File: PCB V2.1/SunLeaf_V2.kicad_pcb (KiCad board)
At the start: 4 copper layers, 77 x 40 mm, 107 parts, among them IC1 ESP_09, J1 20021121-00010C4LF, J10 B4B-PH-K-S(LF)(SN), J11 B4B-PH-K-S(LF)(SN), J12 B4B-PH-K-S(LF)(SN), J13 B4B-PH-K-S(LF)(SN), J14 B4B-PH-K-S(LF)(SN), J15 B4B-PH-K-S(LF)(SN), J16 B4B-PH-K-S(LF)(SN), J2 0475890001-MicroUSBPort, J3 B2B-PH-K-S(LF)(SN), J4 B3B-PH-K-S(LF)(SN), J5 B4B-PH-K-S(LF)(SN), J6 B4B-PH-K-S(LF)(SN), J7 B4B-PH-K-S(LF)(SN), J8 B4B-PH-K-S(LF)(SN), J9 B4B-PH-K-S(LF)(SN), P1 CONN_01X04, Q1 DMG2307L-7, Q2 DMG2307L-7, SW1 B3U-1000P, SW2 B3U-1000P, T1 1909763-1, U1 STM32F446RET6_-_TQFP64, U2 BQ24210DQCT, U3 AZ1117CR-3.3TRG1_1, U4 74HC4052D, U5 PCA9518DBQR, X1 ABM3B8.000MHZB2T, X2 ABS07-32.768KHZ-9-T

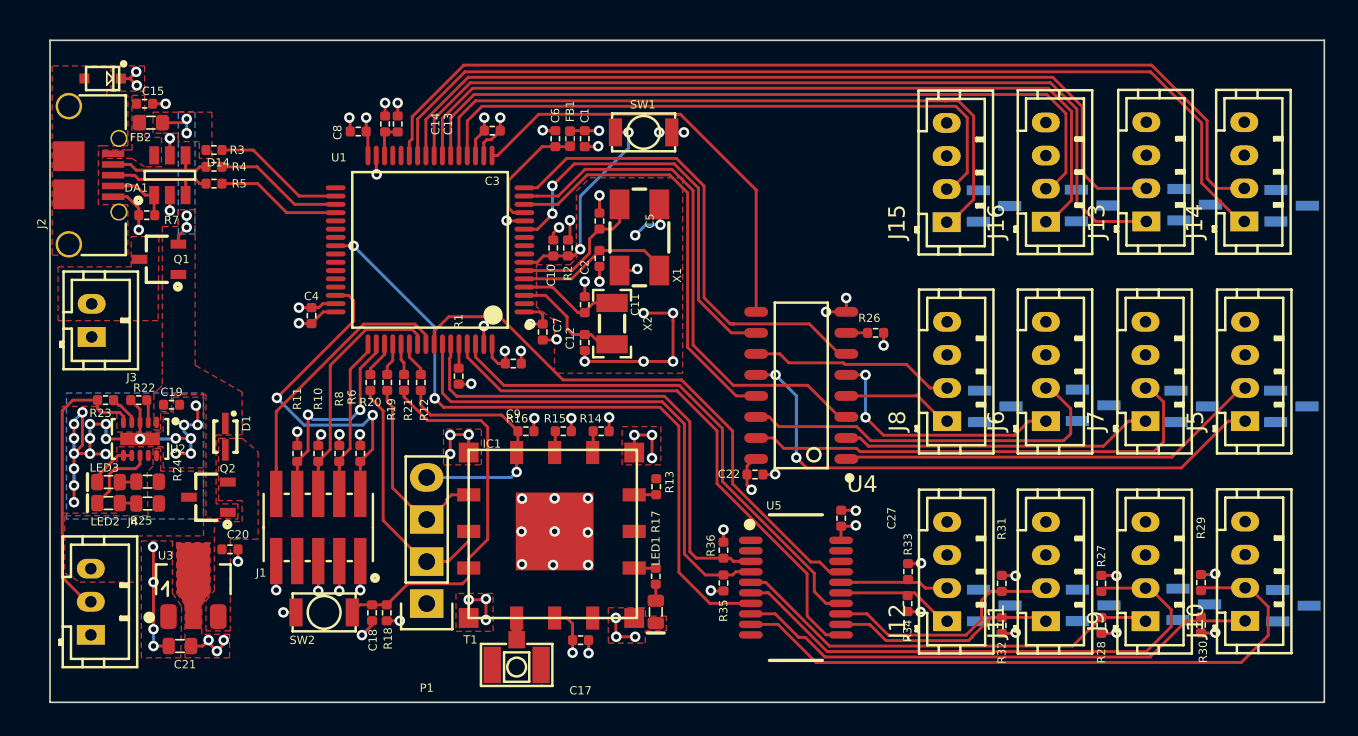
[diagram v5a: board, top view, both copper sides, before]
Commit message: Internal Planes
Internal Planes added, small amount of routing left.
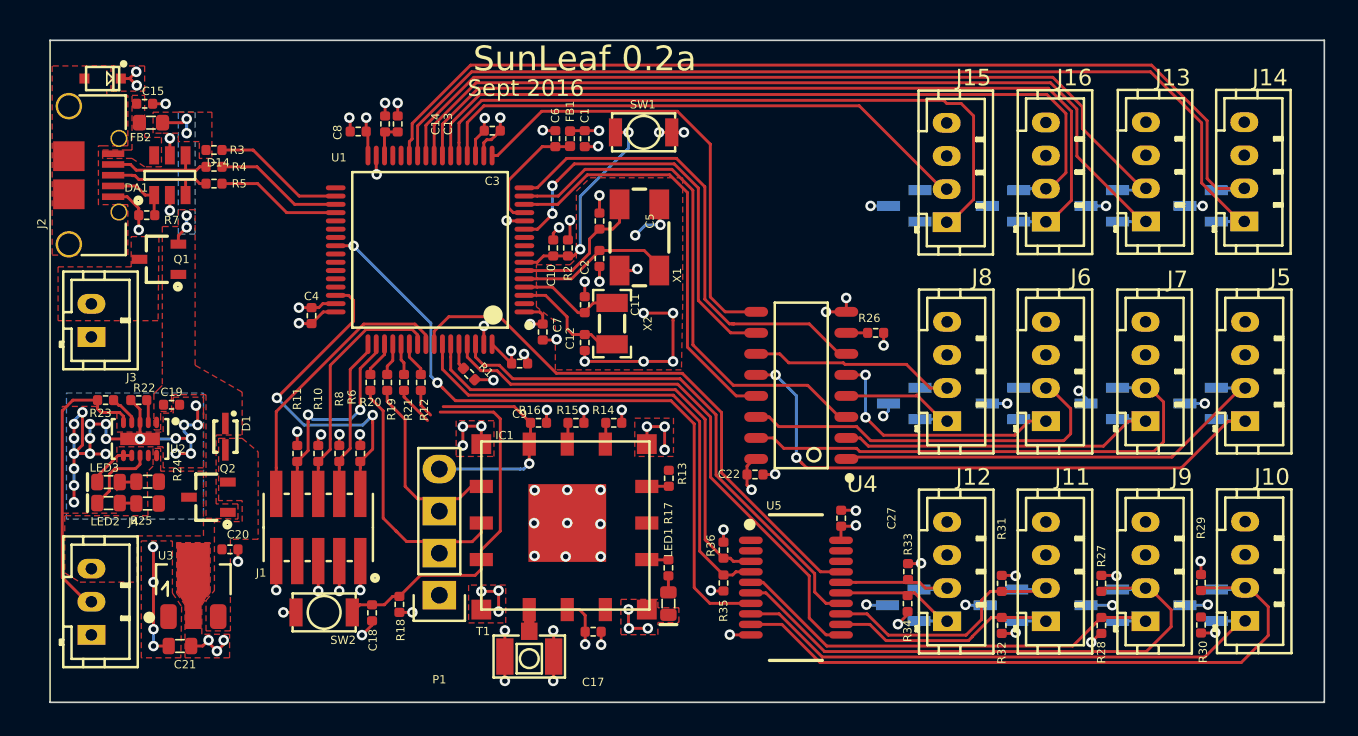
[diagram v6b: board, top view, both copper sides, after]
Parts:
- moved D13 5.61 mm to (106.6, 40.0), turned to 180 degrees
- moved D7 5.61 mm to (112.5, 64.1), turned to 180 degrees
- moved D8 5.57 mm to (100.5, 64.1), turned to 180 degrees
- moved D6 5.56 mm to (106.6, 64.1), turned to 180 degrees
- moved D2 5.51 mm to (94.6, 51.9), turned to 180 degrees
- moved D9 5.51 mm to (94.6, 64.1), turned to 180 degrees
- moved D12 5.50 mm to (112.5, 40.0), turned to 180 degrees
- moved D5 5.49 mm to (112.5, 51.9), turned to 180 degrees
- moved D4 5.45 mm to (100.6, 51.9), turned to 180 degrees
- moved D3 5.44 mm to (106.6, 51.9), turned to 180 degrees
- moved D11 5.43 mm to (94.6, 40.0), turned to 180 degrees
- moved D10 5.38 mm to (100.6, 40.0), turned to 180 degrees
- moved IC1 0.92 mm to (69.1, 64.4)
- moved R18 0.92 mm to (64.1, 64.1)
- moved P1 0.92 mm to (66.5, 63.5)
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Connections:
- D10 pad 1: /Analog and Digital Grove IO/ANIO_7 -> /Analog and Digital Grove IO/ANIO_6
- D10 pad 2: /Analog and Digital Grove IO/ANIO_6 -> /Analog and Digital Grove IO/ANIO_7
- D11 pad 1: /Analog and Digital Grove IO/ANIO_5 -> /Analog and Digital Grove IO/ANIO_4
- D11 pad 2: /Analog and Digital Grove IO/ANIO_4 -> /Analog and Digital Grove IO/ANIO_5
- D12 pad 1: /Analog and Digital Grove IO/ANIO_3 -> /Analog and Digital Grove IO/ANIO_2
- D12 pad 2: /Analog and Digital Grove IO/ANIO_2 -> /Analog and Digital Grove IO/ANIO_3
- D13 pad 1: /Analog and Digital Grove IO/ANIO_1 -> /Analog and Digital Grove IO/ANIO_0
- D13 pad 2: /Analog and Digital Grove IO/ANIO_0 -> /Analog and Digital Grove IO/ANIO_1
- D2 pad 1: /UART Grove Sensors/UART_RX3 -> /UART Grove Sensors/UART_TX3
- D2 pad 2: /UART Grove Sensors/UART_TX3 -> /UART Grove Sensors/UART_RX3
- D3 pad 1: /UART Grove Sensors/UART_RX2 -> /UART Grove Sensors/UART_TX2
- D3 pad 2: /UART Grove Sensors/UART_TX2 -> /UART Grove Sensors/UART_RX2
- D4 pad 1: /UART Grove Sensors/UART_RX1 -> /UART Grove Sensors/UART_TX1
- D4 pad 2: /UART Grove Sensors/UART_TX1 -> /UART Grove Sensors/UART_RX1
- D5 pad 1: /UART Grove Sensors/UART_RX0 -> /UART Grove Sensors/UART_TX0
- D5 pad 2: /UART Grove Sensors/UART_TX0 -> /UART Grove Sensors/UART_RX0
- J10 pad 1: Net-(D7-Pad1) -> Net-(D7-Pad2)
- J10 pad 2: Net-(D7-Pad2) -> Net-(D7-Pad1)
- J11 pad 1: Net-(D8-Pad1) -> Net-(D8-Pad2)
- J11 pad 2: Net-(D8-Pad2) -> Net-(D8-Pad1)
- J12 pad 1: Net-(D9-Pad1) -> Net-(D9-Pad2)
- J12 pad 2: Net-(D9-Pad2) -> Net-(D9-Pad1)
- J9 pad 1: Net-(D6-Pad1) -> Net-(D6-Pad2)
- J9 pad 2: Net-(D6-Pad2) -> Net-(D6-Pad1)
- R27 pad 2: Net-(D6-Pad2) -> Net-(D6-Pad1)
- R28 pad 2: Net-(D6-Pad1) -> Net-(D6-Pad2)
- R29 pad 2: Net-(D7-Pad2) -> Net-(D7-Pad1)
- R30 pad 2: Net-(D7-Pad1) -> Net-(D7-Pad2)
- R31 pad 2: Net-(D8-Pad2) -> Net-(D8-Pad1)
- R32 pad 2: Net-(D8-Pad1) -> Net-(D8-Pad2)
- R33 pad 2: Net-(D9-Pad2) -> Net-(D9-Pad1)
- R34 pad 2: Net-(D9-Pad1) -> Net-(D9-Pad2)
- U5 pad 12: Net-(D8-Pad1) -> Net-(D8-Pad2)
- U5 pad 13: Net-(D8-Pad2) -> Net-(D8-Pad1)
- U5 pad 15: Net-(D9-Pad1) -> Net-(D9-Pad2)
- U5 pad 16: Net-(D9-Pad2) -> Net-(D9-Pad1)
- U5 pad 5: Net-(D6-Pad1) -> Net-(D6-Pad2)
- U5 pad 6: Net-(D6-Pad2) -> Net-(D6-Pad1)
- U5 pad 8: Net-(D7-Pad1) -> Net-(D7-Pad2)
- U5 pad 9: Net-(D7-Pad2) -> Net-(D7-Pad1)
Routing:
- net GND: track 120.2 -> 139.3 mm, vias 92 -> 107
- net Net-(D7-Pad1): track 31.9 -> 41.0 mm
- net Net-(D6-Pad1): track 26.3 -> 35.1 mm
- net Net-(D7-Pad2): track 39.2 -> 33.6 mm
- net Net-(D6-Pad2): track 33.4 -> 28.0 mm
- net /Analog and Digital Grove IO/ANIO_4: track 38.0 -> 33.5 mm
- net Net-(D8-Pad1): track 13.5 -> 16.6 mm
- net Net-(D9-Pad2): track 6.73 -> 8.83 mm
- net /UART Grove Sensors/UART_RX0: track 35.4 -> 37.2 mm
- net /UART Grove Sensors/UART_TX0: track 26.0 -> 27.7 mm
- net /UART Grove Sensors/UART_RX2: track 19.0 -> 20.8 mm
- net /UART Grove Sensors/UART_TX2: track 29.2 -> 30.9 mm
- net /UART Grove Sensors/UART_RX3: track 6.88 -> 8.57 mm
- net /UART Grove Sensors/UART_TX3: track 12.5 -> 14.2 mm
- net Net-(D6-Pad3): track 0.00 -> 1.59 mm, vias 0 -> 1
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- added copper zone on In2.Cu, net +3V3
- added copper zone on In1.Cu, net GND
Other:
- board text added: "Sept 2016"
- board text added: "SunLeaf 0.2a"

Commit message: PDF
Schematic PDF updated.
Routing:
- net Net-(C18-Pad1): track 24.6 -> 25.3 mm
- net /WiFi-ESP8266-ESP-09/PGM_MODE: track 15.5 -> 16.1 mm
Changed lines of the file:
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@@
     (thickness 1.6)
     (drawings 16)
-    (tracks 1002)
+    (tracks 1004)
     (zones 0)
     (modules 107)
@@
   (segment (start 63.208829 36.957872) (end 63.211457 36.9605) (width 0.1778) (layer F.Cu) (net 9))
   (segment (start 64.008 35.535) (end 63.246 35.535) (width 0.1778) (layer F.Cu) (net 9))
-  (segment (start 64.1096 63.6008) (end 63.7046 63.6008) (width 0.1778) (layer F.Cu) (net 11))
-  (segment (start 63.7046 63.6008) (end 63.1966 64.1088) (width 0.1778) (layer F.Cu) (net 11))
-  (segment (start 63.1966 64.1088) (end 62.4586 64.1088) (width 0.1778) (layer F.Cu) (net 11))
-  (segment (start 64.389 51.156) (end 64.389 51.54744) (width 0.1778) (layer F.Cu) (net 11))
-  (segment (start 64.389 51.54744) (end 65.812713 52.971153) (width 0.1778) (layer F.Cu) (net 11))
-  (segment (start 66.574713 52.463153) (end 69.801567 52.463153) (width 0.1778) (layer F.Cu) (net 11))
+  (segment (start 64.389 51.156) (end 64.389 51.788336) (width 0.1778) (layer F.Cu) (net 11))
+  (segment (start 64.389 51.788336) (end 65.063817 52.463153) (width 0.1778) (layer F.Cu) (net 11))
+  (segment (start 65.063817 52.463153) (end 69.801567 52.463153) (width 0.1778) (layer F.Cu) (net 11))
   (segment (start 69.801567 52.463153) (end 70.205528 52.867114) (width 0.1778) (layer F.Cu) (net 11))
   (segment (start 70.205528 52.867114) (end 70.205528 59.651772) (width 0.1778) (layer F.Cu) (net 11))
   (segment (start 70.205528 59.651772) (end 69.0601 60.7972) (width 0.1778) (layer F.Cu) (net 11))
   (segment (start 69.0601 60.7972) (end 69.0601 61.375) (width 0.1778) (layer F.Cu) (net 11))
+  (segment (start 64.1096 63.6008) (end 63.7046 63.6008) (width 0.1778) (layer F.Cu) (net 11))
+  (segment (start 63.7046 63.6008) (end 63.1966 64.1088) (width 0.1778) (layer F.Cu) (net 11))
+  (segment (start 63.1966 64.1088) (end 62.4586 64.1088) (width 0.1778) (layer F.Cu) (net 11))
   (segment (start 69.0601 61.375) (end 69.0601 61.9528) (width 0.1778) (layer F.Cu) (net 11))
   (segment (start 69.0601 61.9528) (end 68.6813 62.3316) (width 0.1778) (layer F.Cu) (net 11))
@@
   (segment (start 74.2946 53.1114) (end 74.2946 54.3575) (width 0.1778) (layer F.Cu) (net 39))
   (segment (start 74.2946 54.3575) (end 74.2541 54.398) (width 0.1778) (layer F.Cu) (net 39))
-  (segment (start 72.0336 53.1114) (end 71.055142 52.132942) (width 0.1778) (layer F.Cu) (net 40))
-  (segment (start 71.055142 52.132942) (end 66.757778 52.132942) (width 0.1778) (layer F.Cu) (net 40))
-  (segment (start 65.995778 52.640942) (end 65.405 52.050164) (width 0.1778) (layer F.Cu) (net 40))
-  (segment (start 65.405 52.050164) (end 65.405 51.156) (width 0.1778) (layer F.Cu) (net 40))
-  (segment (start 71.9582 55.5752) (end 71.626994 55.906406) (width 0.1778) (layer B.Cu) (net 40))
-  (segment (start 71.626994 55.906406) (end 71.41671 55.906406) (width 0.1778) (layer B.Cu) (net 40))
-  (segment (start 71.41671 55.906406) (end 71.415704 55.9054) (width 0.1778) (layer B.Cu) (net 40))
-  (segment (start 71.415704 55.9054) (end 66.5226 55.9054) (width 0.1778) (layer B.Cu) (net 40))
+  (segment (start 71.9582 55.5752) (end 71.415723 56.117677) (width 0.1778) (layer B.Cu) (net 40))
+  (segment (start 71.415723 56.117677) (end 66.734877 56.117677) (width 0.1778) (layer B.Cu) (net 40))
+  (segment (start 66.734877 56.117677) (end 66.5226 55.9054) (width 0.1778) (layer B.Cu) (net 40))
+  (segment (start 71.12 52.1978) (end 71.055143 52.132943) (width 0.1778) (layer F.Cu) (net 40))
+  (segment (start 71.055143 52.132943) (end 65.803768 52.132943) (width 0.1778) (layer F.Cu) (net 40))
+  (segment (start 65.803768 52.132943) (end 65.397642 51.726817) (width 0.1778) (layer F.Cu) (net 40))
+  (segment (start 65.397642 51.726817) (end 65.397642 51.163358) (width 0.1778) (layer F.Cu) (net 40))
+  (segment (start 65.397642 51.163358) (end 65.405 51.156) (width 0.1778) (layer F.Cu) (net 40))
+  (segment (start 72.0336 53.1114) (end 71.12 52.1978) (width 0.1778) (layer F.Cu) (net 40))
+  (segment (start 71.12 52.1978) (end 71.055142 52.132942) (width 0.1778) (layer F.Cu) (net 40))
   (segment (start 71.9561 54.398) (end 71.9561 55.5731) (width 0.1778) (layer F.Cu) (net 40))
   (segment (start 71.9561 55.5731) (end 71.9582 55.5752) (width 0.1778) (layer F.Cu) (net 40))

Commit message: Workstation Switch
Switching to laptop, syncing files.
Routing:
- net /MCU-STM32F446RET6/ESP_ST_RST: track 12.8 -> 52.2 mm
- net GND: track 139.3 -> 140.4 mm
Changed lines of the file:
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@@
     (thickness 1.6)
     (drawings 16)
-    (tracks 1004)
+    (tracks 1021)
     (zones 0)
     (modules 107)
@@
   (segment (start 52.2224 66.5988) (end 52.578 66.2432) (width 0.1778) (layer F.Cu) (net 1))
   (via (at 52.578 66.2432) (size 0.635) (drill 0.3302) (layers F.Cu B.Cu) (net 1))
+  (segment (start 69.211457 48.3605) (end 69.211457 47.783923) (width 0.1778) (layer F.Cu) (net 2))
+  (segment (start 69.211457 47.783923) (end 69.560537 47.434843) (width 0.1778) (layer F.Cu) (net 2))
+  (segment (start 69.560537 47.434843) (end 69.929908 47.434843) (width 0.1778) (layer F.Cu) (net 2))
+  (segment (start 69.929908 47.434843) (end 70.132146 47.637081) (width 0.1778) (layer F.Cu) (net 2))
+  (segment (start 70.132146 47.637081) (end 70.449645 47.95458) (width 0.1778) (layer F.Cu) (net 2))
+  (via (at 70.449645 47.95458) (size 0.635) (drill 0.3302) (layers F.Cu B.Cu) (net 2))
   (segment (start 99.634 51.943) (end 100.838 51.943) (width 0.1778) (layer B.Cu) (net 2))
   (via (at 100.838 51.943) (size 0.635) (drill 0.3302) (layers F.Cu B.Cu) (net 2))
@@
   (via (at 86.8172 56.2102) (size 0.635) (drill 0.3302) (layers F.Cu B.Cu) (net 2))
   (segment (start 69.0601 64.398) (end 69.0601 63.2993) (width 0.1778) (layer F.Cu) (net 2))
-  (segment (start 69.0601 63.2993) (end 69.0626 63.2968) (width 0.1778) (layer F.Cu) (net 2))
   (via (at 69.0626 63.2968) (size 0.635) (drill 0.3302) (layers F.Cu B.Cu) (net 2))
   (via (at 79.0702 53.34) (size 0.635) (drill 0.3302) (layers F.Cu B.Cu) (net 2))
@@
   (segment (start 57.863 64.5668) (end 57.0992 64.5668) (width 0.1778) (layer F.Cu) (net 2))
   (via (at 57.0992 64.5668) (size 0.635) (drill 0.3302) (layers F.Cu B.Cu) (net 2))
-  (via (at 69.215 47.25735) (size 0.635) (drill 0.3302) (layers F.Cu B.Cu) (net 2))
-  (segment (start 69.211457 47.260893) (end 69.215 47.25735) (width 0.1778) (layer F.Cu) (net 2))
-  (segment (start 69.211457 48.3605) (end 69.211457 47.260893) (width 0.1778) (layer F.Cu) (net 2))
   (segment (start 73.569721 48.108) (end 73.61118 48.066541) (width 0.1778) (layer F.Cu) (net 2))
   (segment (start 72.771 48.108) (end 73.569721 48.108) (width 0.1778) (layer F.Cu) (net 2))
@@
   (segment (start 73.533 36.424) (end 74.394 36.424) (width 0.1778) (layer F.Cu) (net 5))
   (segment (start 74.394 36.424) (end 74.422 36.396) (width 0.1778) (layer F.Cu) (net 5))
+  (segment (start 80.391 55.9808) (end 80.237799 56.134001) (width 0.1778) (layer F.Cu) (net 6))
+  (segment (start 55.372 60.552058) (end 56.488058 59.436) (width 0.1778) (layer F.Cu) (net 6))
+  (segment (start 56.488058 59.436) (end 56.642 59.436) (width 0.1778) (layer F.Cu) (net 6))
+  (segment (start 80.237799 56.134001) (end 71.881999 56.134001) (width 0.1778) (layer F.Cu) (net 6))
+  (segment (start 71.881999 56.134001) (end 70.993 57.023) (width 0.1778) (layer F.Cu) (net 6))
+  (segment (start 70.993 57.023) (end 70.993 60.976442) (width 0.1778) (layer F.Cu) (net 6))
+  (segment (start 70.993 60.976442) (end 69.485442 62.484) (width 0.1778) (layer F.Cu) (net 6))
+  (segment (start 67.779901 64.582041) (end 65.864741 66.497201) (width 0.1778) (layer F.Cu) (net 6))
+  (segment (start 56.845201 66.497201) (end 55.372 65.024) (width 0.1778) (layer F.Cu) (net 6))
+  (segment (start 69.485442 62.484) (end 68.203861 62.484) (width 0.1778) (layer F.Cu) (net 6))
+  (segment (start 68.203861 62.484) (end 67.779901 62.90796) (width 0.1778) (layer F.Cu) (net 6))
+  (segment (start 67.779901 62.90796) (end 67.779901 64.582041) (width 0.1778) (layer F.Cu) (net 6))
+  (segment (start 65.864741 66.497201) (end 56.845201 66.497201) (width 0.1778) (layer F.Cu) (net 6))
+  (segment (start 55.372 65.024) (end 55.372 60.552058) (width 0.1778) (layer F.Cu) (net 6))
   (segment (start 75.040064 39.429264) (end 77.9526 36.516728) (width 0.1778) (layer B.Cu) (net 6))
   (segment (start 77.9526 36.516728) (end 77.9526 35.56) (width 0.1778) (layer B.Cu) (net 6))
@@
   (segment (start 63.208829 36.957872) (end 63.211457 36.9605) (width 0.1778) (layer F.Cu) (net 9))
   (segment (start 64.008 35.535) (end 63.246 35.535) (width 0.1778) (layer F.Cu) (net 9))
+  (segment (start 64.1096 63.6008) (end 65.462985 62.247415) (width 0.1778) (layer F.Cu) (net 11))
+  (segment (start 65.462985 62.247415) (end 67.574049 62.247415) (width 0.1778) (layer F.Cu) (net 11))
+  (segment (start 67.574049 62.247415) (end 68.446464 61.375) (width 0.1778) (layer F.Cu) (net 11))
+  (segment (start 68.446464 61.375) (end 69.0601 61.375) (width 0.1778) (layer F.Cu) (net 11))
   (segment (start 64.389 51.156) (end 64.389 51.788336) (width 0.1778) (layer F.Cu) (net 11))
   (segment (start 64.389 51.788336) (end 65.063817 52.463153) (width 0.1778) (layer F.Cu) (net 11))
+  (segment (start 69.2783 60.579) (end 69.0601 60.7972) (width 0.1778) (layer F.Cu) (net 11))
   (segment (start 65.063817 52.463153) (end 69.801567 52.463153) (width 0.1778) (layer F.Cu) (net 11))
   (segment (start 69.801567 52.463153) (end 70.205528 52.867114) (width 0.1778) (layer F.Cu) (net 11))
-  (segment (start 70.205528 52.867114) (end 70.205528 59.651772) (width 0.1778) (layer F.Cu) (net 11))
-  (segment (start 70.205528 59.651772) (end 69.0601 60.7972) (width 0.1778) (layer F.Cu) (net 11))
+  (segment (start 70.205528 52.867114) (end 70.205528 60.045528) (width 0.1778) (layer F.Cu) (net 11))
+  (segment (start 70.205528 60.045528) (end 69.672056 60.579) (width 0.1778) (layer F.Cu) (net 11))
+  (segment (start 69.672056 60.579) (end 69.2783 60.579) (width 0.1778) (layer F.Cu) (net 11))
   (segment (start 69.0601 60.7972) (end 69.0601 61.375) (width 0.1778) (layer F.Cu) (net 11))
   (segment (start 64.1096 63.6008) (end 63.7046 63.6008) (width 0.1778) (layer F.Cu) (net 11))
   (segment (start 63.7046 63.6008) (end 63.1966 64.1088) (width 0.1778) (layer F.Cu) (net 11))
   (segment (start 63.1966 64.1088) (end 62.4586 64.1088) (width 0.1778) (layer F.Cu) (net 11))
-  (segment (start 69.0601 61.375) (end 69.0601 61.9528) (width 0.1778) (layer F.Cu) (net 11))
-  (segment (start 69.0601 61.9528) (end 68.6813 62.3316) (width 0.1778) (layer F.Cu) (net 11))
-  (segment (start 68.6813 62.3316) (end 65.3788 62.3316) (width 0.1778) (layer F.Cu) (net 11))
-  (segment (start 65.3788 62.3316) (end 64.1342 63.5762) (width 0.1778) (layer F.Cu) (net 11))
-  (segment (start 64.1342 63.5762) (end 64.1096 63.6008) (width 0.1778) (layer F.Cu) (net 11))
   (segment (start 62.4586 64.1088) (end 61.721 64.1088) (width 0.1778) (layer F.Cu) (net 11))
   (segment (start 61.721 64.1088) (end 61.263 64.5668) (width 0.1778) (layer F.Cu) (net 11))
@@
   (segment (start 61.3335 42.4105) (end 61.341 42.418) (width 0.1778) (layer F.Cu) (net 81))
   (via (at 61.341 42.418) (size 0.635) (drill 0.3302) (layers F.Cu B.Cu) (net 81))
-  (segment (start 70.175051 46.69854) (end 67.095617 46.69854) (width 0.1778) (layer F.Cu) (net 87))
-  (segment (start 73.59444 50.117929) (end 70.175051 46.69854) (width 0.1778) (layer F.Cu) (net 87))
-  (segment (start 81.203188 50.117929) (end 73.59444 50.117929) (width 0.1778) (layer F.Cu) (net 87))
   (segment (start 90.794 62.1152) (end 89.56144 62.1152) (width 0.1778) (layer F.Cu) (net 87))
-  (segment (start 83.575417 52.490158) (end 81.203188 50.117929) (width 0.1778) (layer F.Cu) (net 87))
   (segment (start 89.56144 62.1152) (end 83.575417 56.129177) (width 0.1778) (layer F.Cu) (net 87))
-  (segment (start 67.095617 46.69854) (end 66.211457 47.5827) (width 0.1778) (layer F.Cu) (net 87))
   (segment (start 83.575417 56.129177) (end 83.575417 52.490158) (width 0.1778) (layer F.Cu) (net 87))
+  (segment (start 83.575417 52.490158) (end 81.203188 50.117929) (width 0.1778) (layer F.Cu) (net 87))
+  (segment (start 81.203188 50.117929) (end 73.638494 50.117929) (width 0.1778) (layer F.Cu) (net 87))
   (segment (start 66.211457 47.5827) (end 66.211457 48.3605) (width 0.1778) (layer F.Cu) (net 87))
+  (segment (start 73.638494 50.117929) (end 70.622702 47.102137) (width 0.1778) (layer F.Cu) (net 87))
+  (segment (start 70.622702 47.102137) (end 66.69202 47.102137) (width 0.1778) (layer F.Cu) (net 87))
+  (segment (start 66.69202 47.102137) (end 66.211457 47.5827) (width 0.1778) (layer F.Cu) (net 87))
   (segment (start 68.277383 51.438773) (end 66.711457 49.872847) (width 0.1778) (layer F.Cu) (net 88))
   (segment (start 66.711457 49.872847) (end 66.711457 49.1383) (width 0.1778) (layer F.Cu) (net 88))
